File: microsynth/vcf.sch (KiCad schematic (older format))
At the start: 45 parts, among them Q4 BC212 PNP, Q5 BC212 PNP, Q6 BC548, Q7 BC548, Q8 BC548, SW10 SW_SPST, SW11 SW_SPDT, U19 LM741, U20 LM13600

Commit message: Footprints 2
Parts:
- C21, C22, C23, C24, C25: footprint (none) -> Capacitor_THT:C_Disc_D5.0mm_W2.5mm_P5.00mm
- Q4, Q5: footprint (none) -> Package_TO_SOT_THT:TO-92L_Inline_Wide
- Q6, Q7, Q8: footprint Package_TO_SOT_THT:TO-92_Inline -> Package_TO_SOT_THT:TO-92L_Inline_Wide
- R149_1: footprint (none) -> Resistor_THT:R_Axial_DIN0207_L6.3mm_D2.5mm_P10.16mm_Horizontal
- U19: footprint (none) -> Package_DIP:DIP-8_W7.62mm_LongPads
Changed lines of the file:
@@
 F 0 "Q4" H 3041 2254 50  0000 L CNN
 F 1 "BC212 PNP" H 3041 2345 50  0000 L CNN
-F 2 "" H 3050 2400 50  0001 C CNN
+F 2 "Package_TO_SOT_THT:TO-92L_Inline_Wide" H 3050 2400 50  0001 C CNN
 F 3 "~" H 2850 2300 50  0001 C CNN
 	1    2850 2300
@@
 F 0 "Q5" H 3891 2254 50  0000 L CNN
 F 1 "BC212 PNP" H 3891 2345 50  0000 L CNN
-F 2 "" H 3900 2400 50  0001 C CNN
+F 2 "Package_TO_SOT_THT:TO-92L_Inline_Wide" H 3900 2400 50  0001 C CNN
 F 3 "~" H 3700 2300 50  0001 C CNN
 	1    3700 2300
@@
 F 0 "U19" H 4794 2604 50  0000 L CNN
 F 1 "LM741" H 4794 2695 50  0000 L CNN
-F 2 "" H 4500 2700 50  0001 C CNN
+F 2 "Package_DIP:DIP-8_W7.62mm_LongPads" H 4500 2700 50  0001 C CNN
 F 3 "http://www.ti.com/lit/ds/symlink/lm741.pdf" H 4600 2800 50  0001 C CNN
 	1    4450 2650
@@
 F 0 "C21" V 4198 2150 50  0000 C CNN
 F 1 "100n" V 4289 2150 50  0000 C CNN
-F 2 "" H 4488 2000 50  0001 C CNN
+F 2 "Capacitor_THT:C_Disc_D5.0mm_W2.5mm_P5.00mm" H 4488 2000 50  0001 C CNN
 F 3 "~" H 4450 2150 50  0001 C CNN
 	1    4450 2150
@@
 F 0 "C22" H 3115 5396 50  0000 L CNN
 F 1 "680p" H 3115 5305 50  0000 L CNN
-F 2 "" H 3038 5200 50  0001 C CNN
+F 2 "Capacitor_THT:C_Disc_D5.0mm_W2.5mm_P5.00mm" H 3038 5200 50  0001 C CNN
 F 3 "~" H 3000 5350 50  0001 C CNN
 	1    3000 5350
@@
 F 0 "C23" H 5215 5396 50  0000 L CNN
 F 1 "680p" H 5215 5305 50  0000 L CNN
-F 2 "" H 5138 5200 50  0001 C CNN
+F 2 "Capacitor_THT:C_Disc_D5.0mm_W2.5mm_P5.00mm" H 5138 5200 50  0001 C CNN
 F 3 "~" H 5100 5350 50  0001 C CNN
 	1    5100 5350
@@
 F 0 "R149_1" V 1793 6200 50  0000 C CNN
 F 1 "10k" V 1884 6200 50  0000 C CNN
-F 2 "" V 1930 6200 50  0001 C CNN
+F 2 "Resistor_THT:R_Axial_DIN0207_L6.3mm_D2.5mm_P10.16mm_Horizontal" V 1930 6200 50  0001 C CNN
 F 3 "~" H 2000 6200 50  0001 C CNN
 	1    2000 6200
@@
 F 0 "C24" V 6748 1600 50  0000 C CNN
 F 1 "220n" V 6839 1600 50  0000 C CNN
-F 2 "" H 7038 1450 50  0001 C CNN
+F 2 "Capacitor_THT:C_Disc_D5.0mm_W2.5mm_P5.00mm" H 7038 1450 50  0001 C CNN
 F 3 "~" H 7000 1600 50  0001 C CNN
 	1    7000 1600
@@
 F 0 "C25" V 8648 1300 50  0000 C CNN
 F 1 "100n" V 8739 1300 50  0000 C CNN
-F 2 "" H 8938 1150 50  0001 C CNN
+F 2 "Capacitor_THT:C_Disc_D5.0mm_W2.5mm_P5.00mm" H 8938 1150 50  0001 C CNN
 F 3 "~" H 8900 1300 50  0001 C CNN
 	1    8900 1300
@@
 F 0 "Q6" H 8391 1546 50  0000 L CNN
 F 1 "BC548" H 8391 1455 50  0000 L CNN
-F 2 "Package_TO_SOT_THT:TO-92_Inline" H 8400 1425 50  0001 L CIN
+F 2 "Package_TO_SOT_THT:TO-92L_Inline_Wide" H 8400 1425 50  0001 L CIN
 F 3 "http://www.fairchildsemi.com/ds/BC/BC547.pdf" H 8200 1500 50  0001 L CNN
 	1    8200 1500
@@
 F 0 "Q7" H 9441 1546 50  0000 L CNN
 F 1 "BC548" H 9441 1455 50  0000 L CNN
-F 2 "Package_TO_SOT_THT:TO-92_Inline" H 9450 1425 50  0001 L CIN
+F 2 "Package_TO_SOT_THT:TO-92L_Inline_Wide" H 9450 1425 50  0001 L CIN
 F 3 "http://www.fairchildsemi.com/ds/BC/BC547.pdf" H 9250 1500 50  0001 L CNN
 	1    9250 1500
@@
 F 0 "Q8" H 9891 1454 50  0000 L CNN
 F 1 "BC548" H 9891 1545 50  0000 L CNN
-F 2 "Package_TO_SOT_THT:TO-92_Inline" H 9900 1425 50  0001 L CIN
+F 2 "Package_TO_SOT_THT:TO-92L_Inline_Wide" H 9900 1425 50  0001 L CIN
 F 3 "http://www.fairchildsemi.com/ds/BC/BC547.pdf" H 9700 1500 50  0001 L CNN
 	1    9700 1500

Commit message: Hacking together the footprints
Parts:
- RV21: value 100k -> 100kLIN; footprint (none) -> 4ms_Potentiometer:Pot_16mm_NoDet_RV16AF-4A
- RV22: footprint (none) -> Potentiometers:Potentiometer_Trimmer_Bourns_PV36W
- RV23: value 1k -> 1kLIN; footprint (none) -> 4ms_Potentiometer:Pot_16mm_NoDet_RV16AF-4A
- RV24: value 10k -> 10kLOG; footprint (none) -> 4ms_Potentiometer:Pot_16mm_NoDet_RV16AF-4A
- SW10, SW11: footprint (none) -> 4ms:SPDT_KIT
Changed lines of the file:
@@
 F 0 "RV22" V 2085 2950 50  0000 C CNN
 F 1 "100k" V 1994 2950 50  0000 C CNN
-F 2 "" H 2200 2950 50  0001 C CNN
+F 2 "Potentiometers:Potentiometer_Trimmer_Bourns_PV36W" H 2200 2950 50  0001 C CNN
 F 3 "~" H 2200 2950 50  0001 C CNN
 	1    2200 2950
@@
 F 0 "SW10" H 1750 3275 50  0000 C CNN
 F 1 "SW_SPST" H 1750 3184 50  0000 C CNN
-F 2 "" H 1750 2950 50  0001 C CNN
+F 2 "4ms:SPDT_KIT" H 1750 2950 50  0001 C CNN
 F 3 "~" H 1750 2950 50  0001 C CNN
 F 4 "VCF Keyboard Track" H 1750 3093 50  0000 C CNN "Label"
@@
 P 3400 1350
 F 0 "RV21" H 3330 1259 50  0000 R CNN
-F 1 "100k" H 3330 1350 50  0000 R CNN
-F 2 "" H 3400 1350 50  0001 C CNN
+F 1 "100kLIN" H 3330 1350 50  0000 R CNN
+F 2 "4ms_Potentiometer:Pot_16mm_NoDet_RV16AF-4A" H 3400 1350 50  0001 C CNN
 F 3 "~" H 3400 1350 50  0001 C CNN
 F 4 "VCF Frequency" H 3330 1441 50  0000 R CNN "Label"
@@
 P 1550 6450
 F 0 "RV23" V 1435 6450 50  0000 C CNN
-F 1 "1k" V 1344 6450 50  0000 C CNN
-F 2 "" H 1550 6450 50  0001 C CNN
+F 1 "1kLIN" V 1344 6450 50  0000 C CNN
+F 2 "4ms_Potentiometer:Pot_16mm_NoDet_RV16AF-4A" H 1550 6450 50  0001 C CNN
 F 3 "~" H 1550 6450 50  0001 C CNN
 	1    1550 6450
@@
 F 0 "SW11" H 4200 6925 50  0000 C CNN
 F 1 "SW_SPDT" H 4200 6834 50  0000 C CNN
-F 2 "" H 4200 6550 50  0001 C CNN
+F 2 "4ms:SPDT_KIT" H 4200 6550 50  0001 C CNN
 F 3 "~" H 4200 6550 50  0001 C CNN
 F 4 "VCF MODE" H 4200 6743 50  0000 C CNN "Label"
@@
 P 7450 1600
 F 0 "RV24" H 7380 1509 50  0000 R CNN
-F 1 "10k" H 7380 1600 50  0000 R CNN
-F 2 "" H 7450 1600 50  0001 C CNN
+F 1 "10kLOG" H 7380 1600 50  0000 R CNN
+F 2 "4ms_Potentiometer:Pot_16mm_NoDet_RV16AF-4A" H 7450 1600 50  0001 C CNN
 F 3 "~" H 7450 1600 50  0001 C CNN
 F 4 "Noise Level" H 7380 1691 50  0000 R CNN "Label"

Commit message: All components placed on PCB
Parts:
- renumbered R149_1 to R115
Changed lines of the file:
@@
 $EndComp
 $Comp
-L Device:R R149_1
+L Device:R R115
 U 1 1 5E0EE042
 P 2000 6200
-F 0 "R149_1" V 1793 6200 50  0000 C CNN
+F 0 "R115" V 1793 6200 50  0000 C CNN
 F 1 "10k" V 1884 6200 50  0000 C CNN
 F 2 "Resistor_THT:R_Axial_DIN0207_L6.3mm_D2.5mm_P10.16mm_Horizontal" V 1930 6200 50  0001 C CNN

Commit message: Laying out pcb ...
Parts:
- Q4, Q5: symbol Device:Q_PNP_BCE -> Device:Q_PNP_ECB
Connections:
- net GND: now also Q5.3 (B); no longer Q5.1 (B)
- net at R100.1, R101.2, R102.1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: now also Q4.3 (B); no longer Q4.1 (B)
- new net: Q4.1 (E), Q5.1 (E), R148.2
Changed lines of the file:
@@
 	2500 1750 2500 1900
 $Comp
-L Device:Q_PNP_BCE Q4
+L Device:Q_PNP_ECB Q4
 U 1 1 5E068A19
 P 2850 2300
@@
 	1    2850 2300
 	1    0    0    1
-$EndComp
-$Comp
-L Device:Q_PNP_BCE Q5
-U 1 1 5E06A286
-P 3700 2300
-F 0 "Q5" H 3891 2254 50  0000 L CNN
-F 1 "BC212 PNP" H 3891 2345 50  0000 L CNN
-F 2 "Package_TO_SOT_THT:TO-92L_Inline_Wide" H 3900 2400 50  0001 C CNN
-F 3 "~" H 3700 2300 50  0001 C CNN
-	1    3700 2300
-	-1   0    0    1
 $EndComp
 Wire Wire Line
@@
 Wire Wire Line
 	1350 7000 1100 7000
+$Comp
+L Device:Q_PNP_ECB Q5
+U 1 1 5E06A286
+P 3700 2300
+F 0 "Q5" H 3891 2254 50  0000 L CNN
+F 1 "BC212 PNP" H 3891 2345 50  0000 L CNN
+F 2 "Package_TO_SOT_THT:TO-92L_Inline_Wide" H 3900 2400 50  0001 C CNN
+F 3 "~" H 3700 2300 50  0001 C CNN
+	1    3700 2300
+	-1   0    0    1
+$EndComp
 $EndSCHEMATC

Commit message: Layout...
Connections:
- net LFO_MOD renamed LFO_MOD_S16
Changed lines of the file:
@@
 	2050 2250 1800 2250
 Text GLabel 1800 1600 0    50   BiDi ~ 0
-LFO_MOD
+LFO_MOD_S16
 Text GLabel 1800 2250 0    50   BiDi ~ 0
 THUMBWEEL_MOD
@@
 VCF_OUT
 Text GLabel 1250 900  0    50   BiDi ~ 0
-LFO_MOD
+LFO_MOD_S16
 Text GLabel 1400 900  2    50   BiDi ~ 0
 TO_VCF_R99

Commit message: Tidy up, name switches, proper footprints for all trimmers
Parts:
- SW10, SW11: footprint 4ms:SPDT_KIT -> Buttons_Switches_ThroughHole:GF-624-6014
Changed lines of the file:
@@
 F 0 "SW10" H 1750 3275 50  0000 C CNN
 F 1 "SW_SPST" H 1750 3184 50  0000 C CNN
-F 2 "4ms:SPDT_KIT" H 1750 2950 50  0001 C CNN
+F 2 "Buttons_Switches_ThroughHole:GF-624-6014" H 1750 2950 50  0001 C CNN
 F 3 "~" H 1750 2950 50  0001 C CNN
 F 4 "VCF Keyboard Track" H 1750 3093 50  0000 C CNN "Label"
@@
 F 0 "SW11" H 4200 6925 50  0000 C CNN
 F 1 "SW_SPDT" H 4200 6834 50  0000 C CNN
-F 2 "4ms:SPDT_KIT" H 4200 6550 50  0001 C CNN
+F 2 "Buttons_Switches_ThroughHole:GF-624-6014" H 4200 6550 50  0001 C CNN
 F 3 "~" H 4200 6550 50  0001 C CNN
 F 4 "VCF MODE" H 4200 6743 50  0000 C CNN "Label"

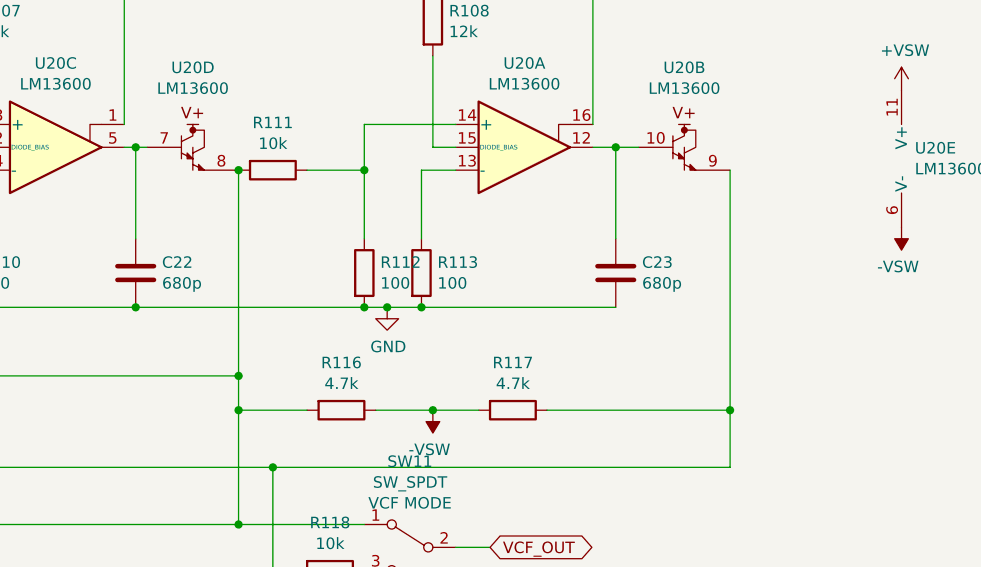
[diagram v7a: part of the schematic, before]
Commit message: Proper capacitor footprints
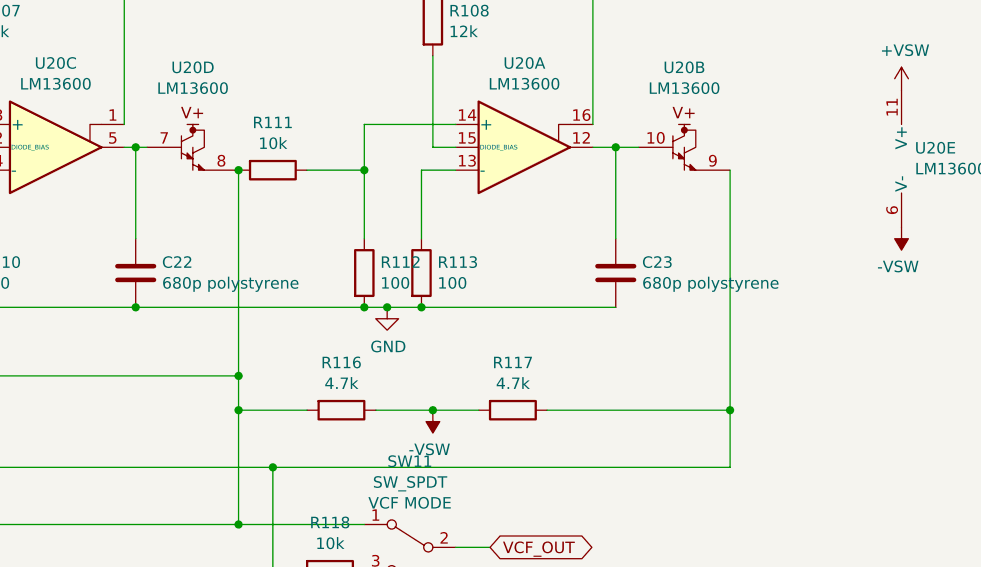
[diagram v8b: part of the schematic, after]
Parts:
- C21, C24, C25: footprint Capacitor_THT:C_Disc_D5.0mm_W2.5mm_P5.00mm -> Capacitor_THT:C_Rect_L7.2mm_W2.5mm_P5.00mm_FKS2_FKP2_MKS2_MKP2
- C22, C23: value 680p -> 680p polystyrene; footprint Capacitor_THT:C_Disc_D5.0mm_W2.5mm_P5.00mm -> Capacitor_THT:C_Axial_L12.0mm_D6.5mm_P15.00mm_Horizontal
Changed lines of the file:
@@
 F 0 "C21" V 4198 2150 50  0000 C CNN
 F 1 "100n" V 4289 2150 50  0000 C CNN
-F 2 "Capacitor_THT:C_Disc_D5.0mm_W2.5mm_P5.00mm" H 4488 2000 50  0001 C CNN
+F 2 "Capacitor_THT:C_Rect_L7.2mm_W2.5mm_P5.00mm_FKS2_FKP2_MKS2_MKP2" H 4488 2000 50  0001 C CNN
 F 3 "~" H 4450 2150 50  0001 C CNN
 	1    4450 2150
@@
 P 3000 5350
 F 0 "C22" H 3115 5396 50  0000 L CNN
-F 1 "680p" H 3115 5305 50  0000 L CNN
-F 2 "Capacitor_THT:C_Disc_D5.0mm_W2.5mm_P5.00mm" H 3038 5200 50  0001 C CNN
-F 3 "~" H 3000 5350 50  0001 C CNN
+F 1 "680p polystyrene" H 3115 5305 50  0000 L CNN
+F 2 "Capacitor_THT:C_Axial_L12.0mm_D6.5mm_P15.00mm_Horizontal" H 3038 5200 50  0001 C CNN
+F 3 "https://uk.rs-online.com/web/p/polystyrene-film-capacitors/0116256/" H 3000 5350 50  0001 C CNN
 	1    3000 5350
 	1    0    0    -1
@@
 P 5100 5350
 F 0 "C23" H 5215 5396 50  0000 L CNN
-F 1 "680p" H 5215 5305 50  0000 L CNN
-F 2 "Capacitor_THT:C_Disc_D5.0mm_W2.5mm_P5.00mm" H 5138 5200 50  0001 C CNN
-F 3 "~" H 5100 5350 50  0001 C CNN
+F 1 "680p polystyrene" H 5215 5305 50  0000 L CNN
+F 2 "Capacitor_THT:C_Axial_L12.0mm_D6.5mm_P15.00mm_Horizontal" H 5138 5200 50  0001 C CNN
+F 3 "https://uk.rs-online.com/web/p/polystyrene-film-capacitors/0116256/" H 5100 5350 50  0001 C CNN
 	1    5100 5350
 	1    0    0    -1
@@
 F 0 "C24" V 6748 1600 50  0000 C CNN
 F 1 "220n" V 6839 1600 50  0000 C CNN
-F 2 "Capacitor_THT:C_Disc_D5.0mm_W2.5mm_P5.00mm" H 7038 1450 50  0001 C CNN
+F 2 "Capacitor_THT:C_Rect_L7.2mm_W2.5mm_P5.00mm_FKS2_FKP2_MKS2_MKP2" H 7038 1450 50  0001 C CNN
 F 3 "~" H 7000 1600 50  0001 C CNN
 	1    7000 1600
@@
 F 0 "C25" V 8648 1300 50  0000 C CNN
 F 1 "100n" V 8739 1300 50  0000 C CNN
-F 2 "Capacitor_THT:C_Disc_D5.0mm_W2.5mm_P5.00mm" H 8938 1150 50  0001 C CNN
+F 2 "Capacitor_THT:C_Rect_L7.2mm_W2.5mm_P5.00mm_FKS2_FKP2_MKS2_MKP2" H 8938 1150 50  0001 C CNN
 F 3 "~" H 8900 1300 50  0001 C CNN
 	1    8900 1300
